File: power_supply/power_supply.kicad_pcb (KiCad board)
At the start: 2 copper layers, 100 x 100 mm, 15 parts, among them J1 Conn_01x02_Female, J2 Conn_01x03_Male, J6 Conn_01x02_Male, J7 Conn_01x02_Male, T1 Transformer_1P_2S

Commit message: More layout
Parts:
- added H1: MountingHole, MountingHole:MountingHole_3.2mm_M3_DIN965, F.Cu at (4.00, -96.0)
- added H2: MountingHole, MountingHole:MountingHole_3.2mm_M3_DIN965, F.Cu at (41.0, -96.0)
- added H3: MountingHole, MountingHole:MountingHole_3.2mm_M3_DIN965, F.Cu at (51.2, -120.9)
- added H4: MountingHole, MountingHole:MountingHole_3.2mm_M3_DIN965, F.Cu at (51.2, -113.8)
- D1, D9: moved to B.Cu
- F1: footprint Fuse:Fuseholder_Cylinder-5x20mm_Schurter_0031-8002_Horizontal_Open -> Project-152-Bass-Guitar-Amp.pretty:Keystone-3527-Fuseholder
- moved D9 165.7 mm to (12.0, -15.2), turned to 105 degrees
- moved D8 155.6 mm to (35.0, -24.0), turned to 255 degrees
- moved F3 138.8 mm to (2.00, -25.6), turned to 90 degrees
- moved D1 138.2 mm to (22.2, -32.2)
- moved J2 136.5 mm to (19.8, -14.8), turned to 90 degrees
- moved J7 77.6 mm to (3.00, -17.5), turned to 0 degrees
- moved F1 38.8 mm to (30.3, -78.3)
- moved F2 29.7 mm to (39.5, -25.5)
- moved J6 29.5 mm to (37.0, -17.5), turned to 0 degrees
- moved C1 24.9 mm to (29.5, -32.0), turned to 0 degrees
- moved C39 24.7 mm to (15.2, -32.0), turned to 180 degrees
- moved C8 22.1 mm to (31.0, -21.8), turned to 180 degrees
- moved C2 16.7 mm to (19.2, -21.8), turned to 180 degrees
- moved J1 9.00 mm to (17.0, -91.0)
- moved T1 6.02 mm to (22.5, -56.0)
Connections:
- T1 pad 3: Net-(D1-Pad3) -> Net-(D1-Pad4)
- T1 pad 6: Net-(D1-Pad4) -> Net-(D1-Pad3)
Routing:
- net Net-(F1-Pad1): track 44.1 -> 11.2 mm
- net GND: track 46.5 -> 18.2 mm
- net +12V: track 10.5 -> 35.5 mm
- net Net-(F3-Pad1): track 0.00 -> 24.7 mm
- net -12V: track 10.4 -> 33.0 mm
- net Net-(D1-Pad3): track 0.00 -> 11.3 mm
- net Net-(F2-Pad1): track 0.00 -> 7.32 mm
- net Net-(F1-Pad2): track 11.4 -> 18.7 mm
- net Net-(J1-Pad1): track 14.4 -> 20.9 mm
- net Net-(D9-Pad1): track 0.00 -> 4.93 mm
- net Net-(D1-Pad4): track 0.00 -> 4.36 mm
- added copper zone on B.Cu, net GND
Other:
- board size 100 x 100 mm -> 45 x 100 mm

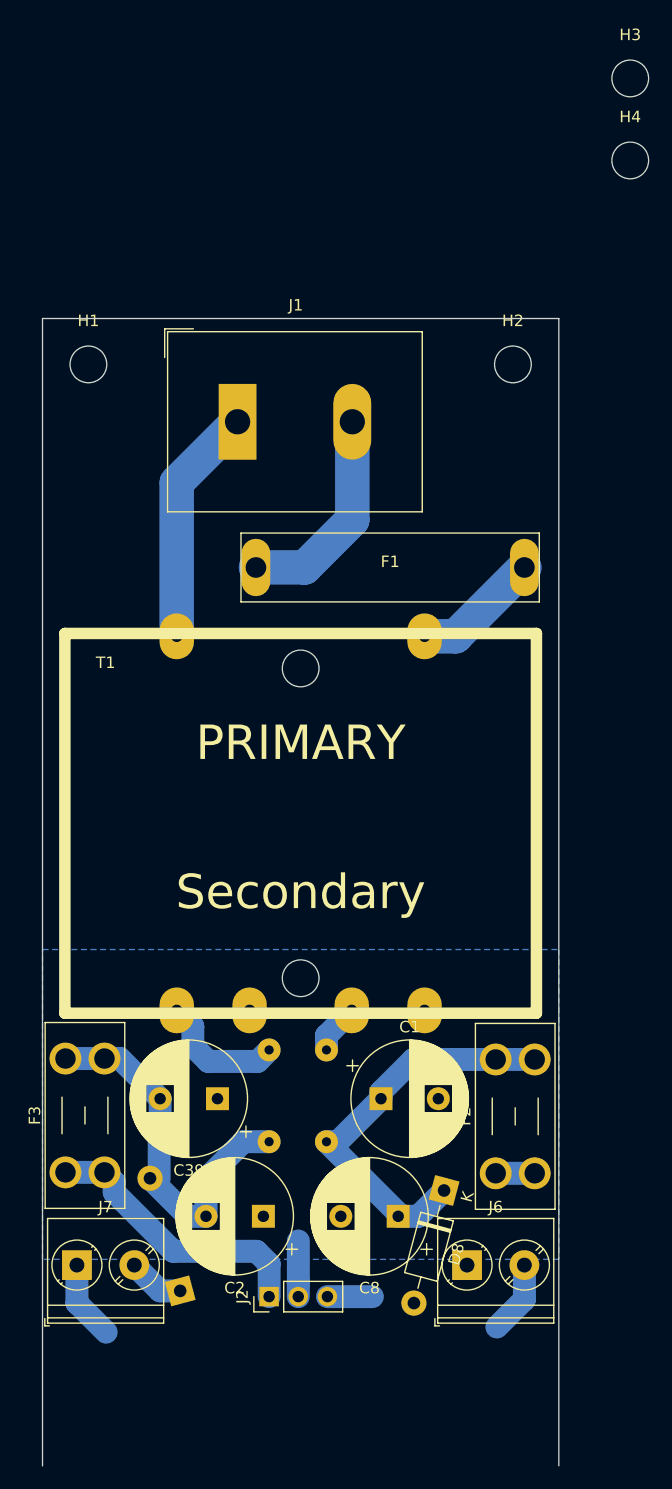
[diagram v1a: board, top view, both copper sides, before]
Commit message: Finished power supply layout, sent out for first rev of boards
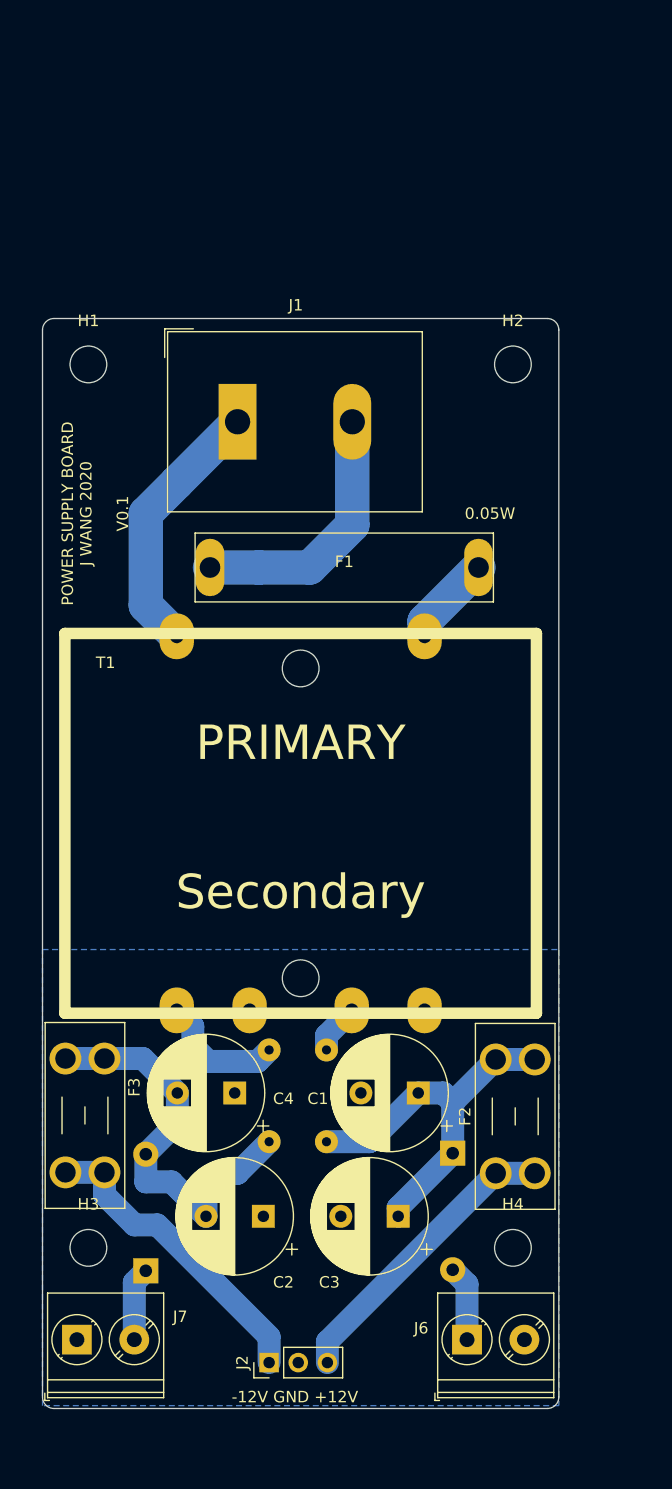
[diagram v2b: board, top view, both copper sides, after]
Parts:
- D8: moved to B.Cu
- moved H3 112.3 mm to (4.00, -19.0)
- moved H4 95.3 mm to (41.0, -19.0)
- moved J6 6.50 mm to (37.0, -11.0)
- moved J7 6.50 mm to (3.00, -11.0)
- moved J2 5.75 mm to (19.8, -9.00)
- moved F1 4.00 mm to (26.3, -78.3)
- moved D9 3.47 mm to (9.00, -17.0), turned to 90 degrees
- moved D8 3.34 mm to (35.8, -27.2), turned to 270 degrees
- moved C1 3.29 mm to (32.8, -32.5), turned to 180 degrees
- moved C4 1.58 mm to (16.8, -32.5)
- renumbered C8 to C3, C39 to C4
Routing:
- net Net-(F2-Pad1): track 7.32 -> 26.0 mm
- net GND: track 18.2 -> 0.00 mm
- net Net-(D8-Pad2): track 0.00 -> 6.61 mm
- net Net-(F1-Pad2): track 18.7 -> 22.9 mm
- net Net-(F1-Pad1): track 11.2 -> 7.95 mm
- net -12V: track 33.0 -> 35.7 mm
- net Net-(F3-Pad1): track 24.7 -> 27.1 mm
- net Net-(J1-Pad1): track 20.9 -> 23.1 mm
- net +12V: track 35.5 -> 33.7 mm
- net Net-(D9-Pad1): track 4.93 -> 6.41 mm
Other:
- board size 45 x 100 mm -> 45 x 95 mm
- board text added: "-12V GND +12V"
- board text added: "0.05W"
- board text added: "POWER SUPPLY BOARD J WANG 2020"
- board text added: "V0.1"
